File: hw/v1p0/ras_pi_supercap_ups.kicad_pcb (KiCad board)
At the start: 2 copper layers, 65 x 56 mm, 85 parts, among them J1 Conn_01x03, J10 Barrel_Jack, J2 Conn_01x05, J3 Conn_01x03, J4 Force Power On, J5 171826-4, J6 LEDs and Buttons, J7 STLinkV2 Connector, J8 Raspberry_Pi_2_3, J9 Test Points, Q1 IRF5305, SW1 Reset, U1 KA431SMFTF, U2 KA431SMFTF, U3 KA431SMFTF, U4 KA431SMFTF, U5 KA431SMFTF, U6 AMS1117-3.3, U7 STM8S003F3P, U8 TPS54331DR

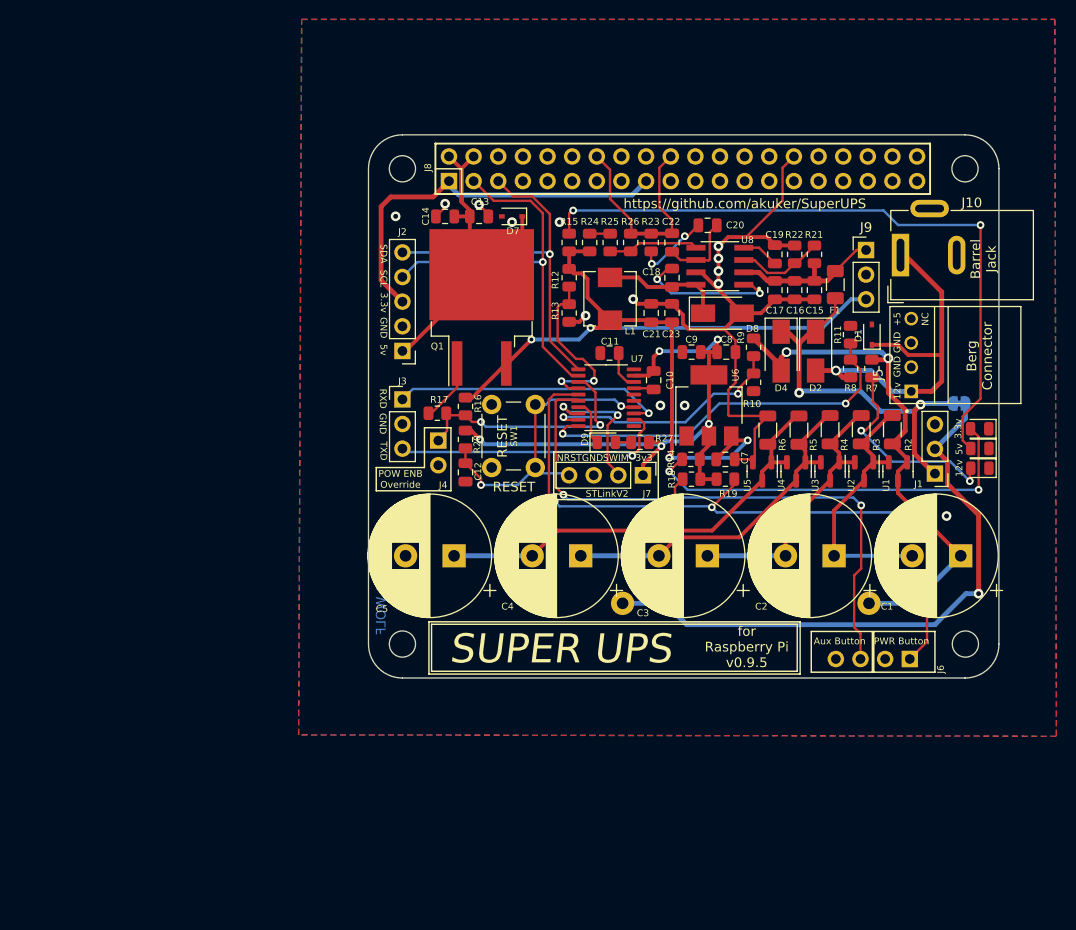
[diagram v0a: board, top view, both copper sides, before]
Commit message: Last version before removing mosfet
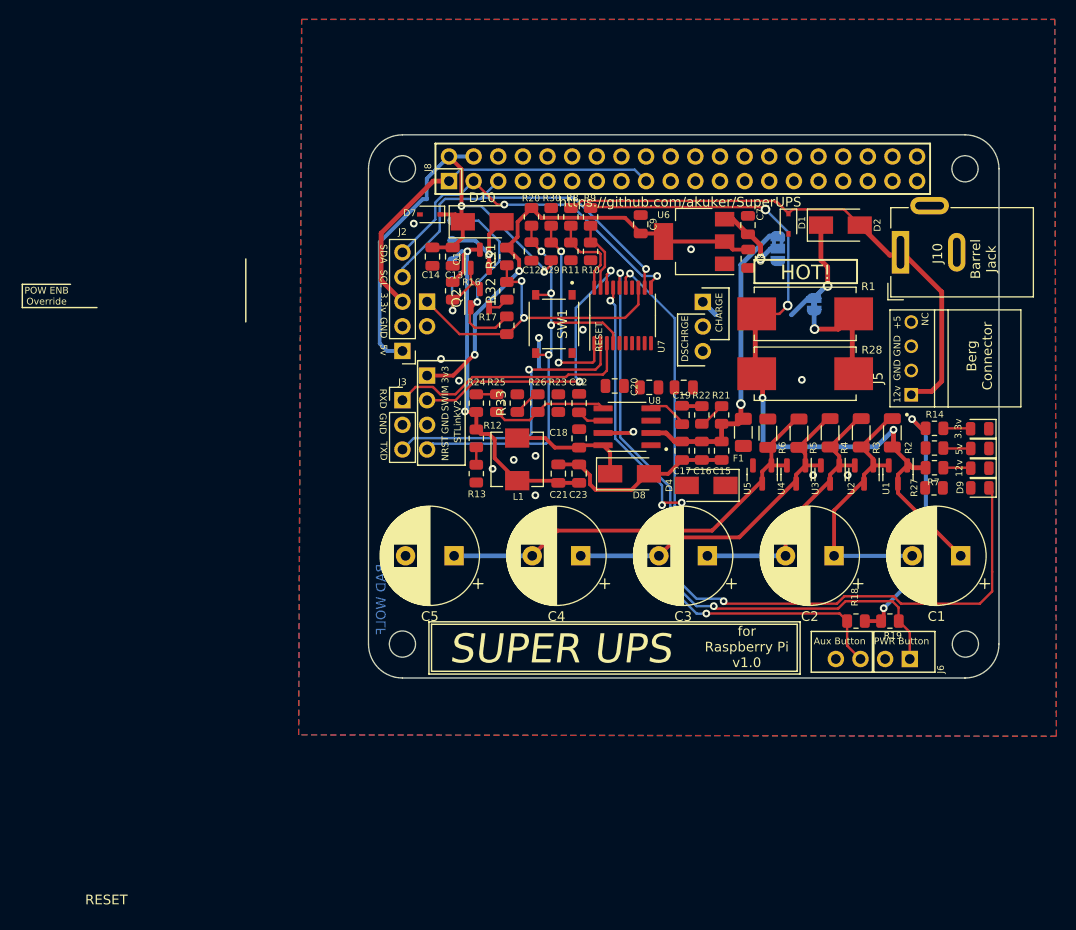
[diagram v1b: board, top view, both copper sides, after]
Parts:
- removed J9: Test Points, Connector_PinHeader_2.54mm:PinHeader_1x03_P2.54mm_Vertical
- added D10: B340LA-13-F, Diode_SMD:D_SMA, F.Cu at (61.7, 109.0)
- added JP2: SolderJumper_3_Bridged12, Jumper:SolderJumper-3_P1.3mm_Bridged2Bar12_RoundedPad1.0x1.5mm_NumberLabels, B.Cu at (92.2, 111.7)
- added Q2: SS8050_SMT, Package_TO_SOT_SMD:SOT-23, F.Cu at (61.5, 116.8)
- added R28: 10 3W, raspberrypi_supercap_ups_lib:SMT_Resistor_4122, F.Cu at (95.0, 124.6)
- added R29: 10k, Resistor_SMD:R_0805_2012Metric, F.Cu at (68.8, 112.0)
- added R30: 20k, Resistor_SMD:R_0805_2012Metric, F.Cu at (68.8, 108.5)
- added R31: DNP, Resistor_SMD:R_0805_2012Metric, F.Cu at (64.3, 112.5)
- added R32: DNP, Resistor_SMD:R_0805_2012Metric, F.Cu at (64.3, 116.1)
- added R33: 200, Resistor_SMD:R_0805_2012Metric, F.Cu at (65.3, 127.7)
- added TP1: TestPoint_Small, TestPoint:TestPoint_Pad_D1.0mm, B.Cu at (58.6, 108.8)
- added TP2: TestPoint_Small, TestPoint:TestPoint_Pad_D1.0mm, B.Cu at (58.6, 113.0)
- added TP3: TestPoint_Small, TestPoint:TestPoint_Pad_D1.0mm, B.Cu at (58.6, 110.9)
- added TP4: TestPoint_Small, TestPoint:TestPoint_Pad_D1.0mm, B.Cu at (58.6, 115.1)
- C1, C2, C3, C4, C5: footprint Capacitor_THT:CP_Radial_D12.5mm_P5.00mm -> Capacitor_THT:CP_Radial_D10.0mm_P5.00mm
- J1, J4, J7: moved to B.Cu
- Q1: value IRF5305 -> AO3401A; footprint Package_TO_SOT_SMD:TO-263-2 -> Package_TO_SOT_SMD:SOT-23
- R1: footprint Resistor_THT:R_Axial_DIN0516_L15.5mm_D5.0mm_P25.40mm_Horizontal -> raspberrypi_supercap_ups_lib:SMT_Resistor_4122; moved to F.Cu
- R17: value 1k -> 4.7k
- R26: value 2k -> 1.5k
- SW1: footprint Button_Switch_THT:SW_PUSH_6mm_H4.3mm -> raspberrypi_supercap_ups_lib:SW_TS-1187A-B-A-B
- moved R15 43.2 mm to (108.3, 132.3), turned to 0 degrees
- moved D9 38.8 mm to (113.0, 136.4), turned to 180 degrees
- moved R1 35.3 mm to (95.0, 118.5), turned to 180 degrees
- moved R8 32.8 mm to (70.9, 108.5), turned to -90 degrees
- moved R27 30.7 mm to (108.3, 136.4), turned to 0 degrees
- moved R11 30.1 mm to (70.9, 112.0), turned to 90 degrees
- moved J1 29.8 mm to (84.5, 117.2)
- moved R14 25.3 mm to (108.3, 130.3), turned to 0 degrees
- moved J7 24.5 mm to (56.0, 124.8), turned to 180 degrees
- moved C7 24.3 mm to (89.1, 109.3), turned to 90 degrees
- moved R20 23.9 mm to (66.8, 108.5)
- moved C12 23.8 mm to (66.8, 112.0)
- moved R18 22.4 mm to (100.3, 150.1)
- moved R19 22.4 mm to (103.8, 150.1)
- moved R10 21.6 mm to (72.9, 112.0)
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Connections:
- C7 pad 1: +5V -> Net-(C7-Pad1)
- J8 pad 3: I2C_SCL -> I2C_SDA
- J8 pad 5: I2C_SDA -> I2C_SCL
- Q1 pad 2: POW_OUT -> Net-(D10-Pad2)
- R16 pad 2: POW_ENABLE -> Net-(Q1-Pad1)
- R17 pad 2: Net-(Q1-Pad1) -> Net-(R17-Pad2)
- R26 pad 2: GND -> Net-(R26-Pad2)
- U6 pad 3: +5V -> Net-(C7-Pad1)
- U7 pad 1: unconnected-(U7-Pad1) -> POW_OUT_SENSE
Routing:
- net DEBUG_LED: track 4.83 -> 80.1 mm, vias 0 -> 4
- net GND: track 102.9 -> 30.9 mm
- net Net-(D6-Pad2): track 69.4 -> 2.85 mm, vias 2 -> 0
- net +5V: track 93.6 -> 40.8 mm, vias 4 -> 2
- net Net-(J1-Pad2): track 61.7 -> 12.4 mm
- net Net-(D5-Pad2): track 41.2 -> 2.83 mm, vias 2 -> 0
- net VIN_SENSE: track 40.0 -> 9.02 mm, vias 2 -> 0
- net Net-(D2-Pad1): track 39.3 -> 13.4 mm, vias 2 -> 1
- net Net-(C1-Pad1): track 56.1 -> 79.7 mm, vias 2 -> 4
- net POW_OUT: track 34.3 -> 56.4 mm, vias 0 -> 2
- net POW_OUT_SENSE: track 0.00 -> 20.3 mm, vias 0 -> 2
- net Net-(R17-Pad2): track 0.00 -> 20.0 mm, vias 0 -> 1
- net Net-(D3-Pad2): track 21.4 -> 2.85 mm, vias 2 -> 0
- net UPS_SENSE: track 25.6 -> 7.46 mm, vias 2 -> 0
- net SWIM: track 14.7 -> 31.6 mm
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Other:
- board text added: "PWR EN"
- board text added: "PWR OUT"
- board text added: "for Raspberry Pi v1.0"
- board text removed: "for Raspberry Pi v0.9.5"

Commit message: Removed Mosfet - release candidate 1.0
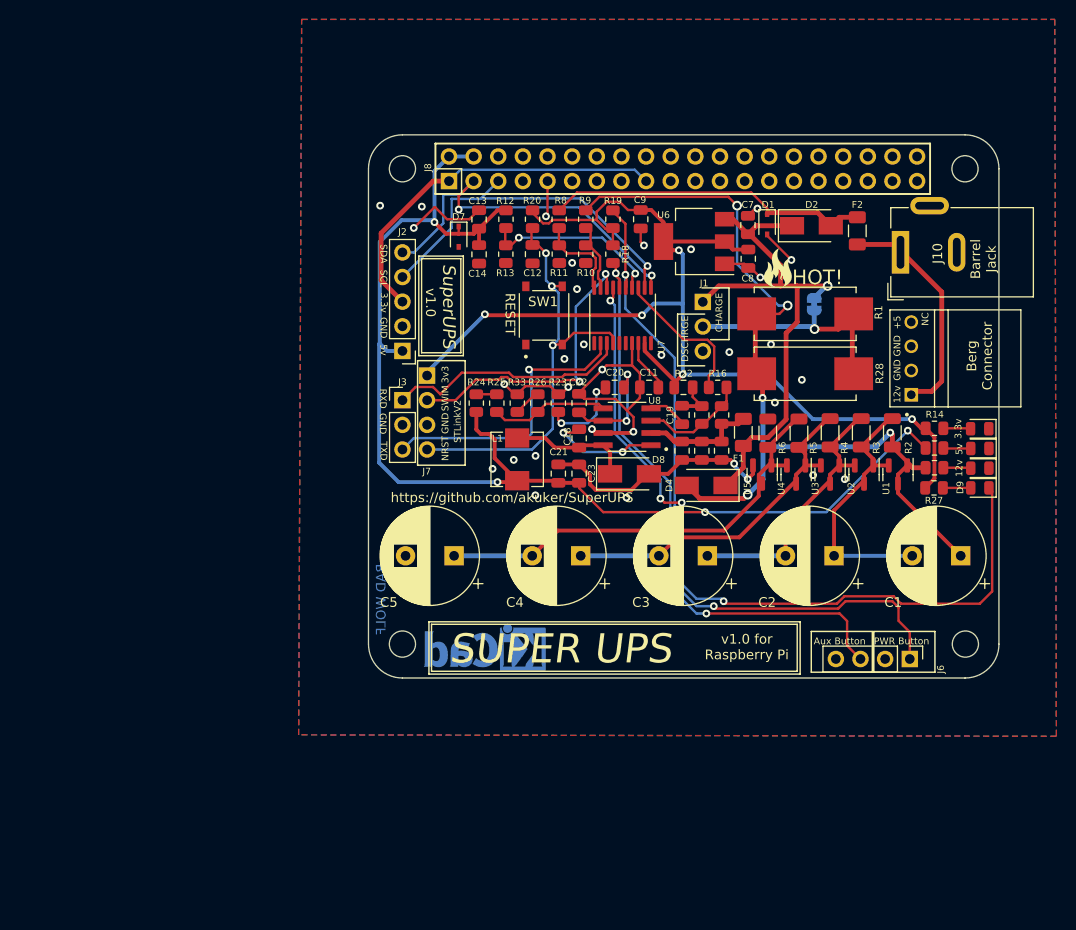
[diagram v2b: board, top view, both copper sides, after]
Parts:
- removed D10: B340LA-13-F, Diode_SMD:D_SMA
- removed J4: Force Power On, Connector_PinHeader_2.54mm:PinHeader_1x02_P2.54mm_Vertical
- removed JP2: SolderJumper_3_Bridged12, Jumper:SolderJumper-3_P1.3mm_Bridged2Bar12_RoundedPad1.0x1.5mm_NumberLabels
- removed Q1: AO3401A, Package_TO_SOT_SMD:SOT-23
- removed Q2: SS8050_SMT, Package_TO_SOT_SMD:SOT-23
- removed R17: 4.7k, Resistor_SMD:R_0805_2012Metric
- removed R29: 10k, Resistor_SMD:R_0805_2012Metric
- removed R30: 20k, Resistor_SMD:R_0805_2012Metric
- removed R31, R32: DNP, Resistor_SMD:R_0805_2012Metric
- removed TP1, TP2, TP3, TP4: TestPoint_Small, TestPoint:TestPoint_Pad_D1.0mm
- added F2: Fuse_Small, Fuse:Fuse_1206_3216Metric, F.Cu at (100.4, 109.9)
- added Z1: SYM_Hot_Small, raspberrypi_supercap_ups_lib:hot_warning_4, F.Cu at (92.2, 113.7)
- added Z2: Logo_Open_Hardware_Small, Symbol:CE-Logo_8.5x6mm_SilkScreen, B.Cu at (55.9, 138.1)
- added Z3: Logo_Open_Hardware_Small, Symbol:KiCad-Logo_5mm_Copper, B.Cu at (62.0, 153.4)
- added Z4: Logo_Open_Hardware_Small, Symbol:OSHW-Logo_7.5x8mm_SilkScreen, B.Cu at (109.8, 137.3)
- R16: value 10k -> 1k
- moved R19 50.3 mm to (75.2, 108.7), turned to 90 degrees
- moved R18 45.4 mm to (75.2, 112.3), turned to -90 degrees
- moved R16 29.1 mm to (86.0, 126.0), turned to 180 degrees
- moved R13 22.8 mm to (64.2, 112.3)
- moved R12 22.8 mm to (64.2, 108.7)
- moved C14 4.81 mm to (61.4, 112.3)
- moved C13 4.70 mm to (61.4, 108.7), turned to 90 degrees
- moved D7 3.74 mm to (59.3, 110.5), turned to -90 degrees
- moved D2 2.99 mm to (95.7, 109.4)
- moved D1 2.20 mm to (91.1, 109.2)
- moved SW1 1.35 mm to (68.1, 118.6), turned to 90 degrees
- moved R8 1.23 mm to (69.7, 108.7)
- moved R11 1.23 mm to (69.7, 112.3)
- moved R10 0.57 mm to (72.4, 112.3)
- moved R9 0.55 mm to (72.4, 108.7)
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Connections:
- C13 pad 1: POW_OUT -> +5V
- C14 pad 1: POW_OUT -> +5V
- C15 pad 1: +12V -> /Buck Converter/VIN_12v
- C16 pad 1: +12V -> /Buck Converter/VIN_12v
- C17 pad 1: +12V -> /Buck Converter/VIN_12v
- C7 pad 1: Net-(C7-Pad1) -> +12V
- D1 pad 1: VIN -> Net-(D1-Pad1)
- D2 pad 1: Net-(D2-Pad1) -> +12V
- D2 pad 2: VIN -> Net-(D1-Pad1)
- D4 pad 1: Net-(D2-Pad1) -> +12V
- D7 pad 1: POW_OUT -> +5V
- F1 pad 1: Net-(D2-Pad1) -> +12V
- F1 pad 2: +12V -> /Buck Converter/VIN_12v
- J1 pad 1: Net-(D2-Pad1) -> +12V
- J2 pad 1: POW_OUT -> +5V
- J8 pad 2: POW_OUT -> +5V
- J8 pad 4: POW_OUT -> +5V
- JP1 pad 2: Net-(D2-Pad1) -> +12V
- R16 pad 1: +5V -> Net-(R16-Pad1)
- R16 pad 2: Net-(Q1-Pad1) -> POW_ENABLE
- R21 pad 1: +12V -> /Buck Converter/VIN_12v
- R21 pad 2: Net-(R21-Pad2) -> Net-(R16-Pad1)
- R22 pad 1: Net-(R21-Pad2) -> Net-(R16-Pad1)
- R8 pad 1: VIN -> Net-(D1-Pad1)
- U6 pad 3: Net-(C7-Pad1) -> +12V
- U7 pad 1: POW_OUT_SENSE -> unconnected-(U7-Pad1)
- U8 pad 2: +12V -> /Buck Converter/VIN_12v
- U8 pad 3: Net-(R21-Pad2) -> Net-(R16-Pad1)
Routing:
- net +5V: track 40.8 -> 125.3 mm, vias 2 -> 4
- net POW_OUT: track 56.4 -> 0.00 mm, vias 2 -> 0
- net GND: track 30.9 -> 85.8 mm, vias 14 -> 32
- net +3V3: track 75.3 -> 115.6 mm, vias 4 -> 5
- net Net-(D1-Pad1): track 0.00 -> 33.8 mm
- net VIN: track 55.4 -> 22.9 mm
- net +12V: track 33.0 -> 54.7 mm
- net POW_OUT_SENSE: track 20.3 -> 0.00 mm, vias 2 -> 0
- net Net-(R17-Pad2): track 20.0 -> 0.00 mm, vias 1 -> 0
- net POW_ENABLE: track 33.4 -> 15.2 mm, vias 2 -> 0
- net VOUT_SENSE: track 1.81 -> 18.1 mm, vias 0 -> 2
- net Net-(D2-Pad1): track 13.4 -> 0.00 mm, vias 1 -> 0
- net /Buck Converter/VIN_12v: track 0.00 -> 11.9 mm
- net Net-(J1-Pad2): track 12.4 -> 24.1 mm
- net Net-(C18-Pad2): track 0.00 -> 11.4 mm, vias 0 -> 2
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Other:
- board text added: "SuperUPS"
- board text added: "v1.0"
- board text added: "v1.0 for Raspberry Pi"
- board text removed: "POW ENB Override"
- board text removed: "PWR EN"
- board text removed: "PWR OUT"
- board text removed: "SuperUPS for Raspberry Pi v0.9.5"
